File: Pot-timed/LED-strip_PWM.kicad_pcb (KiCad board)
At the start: 2 copper layers, 29.7 x 10 mm, 14 parts, among them IC1 ATTINY13A-MM, P1 CONN_2, P2 CONN_2, T1 AO3400, U1 MCP1804-SOT23-5

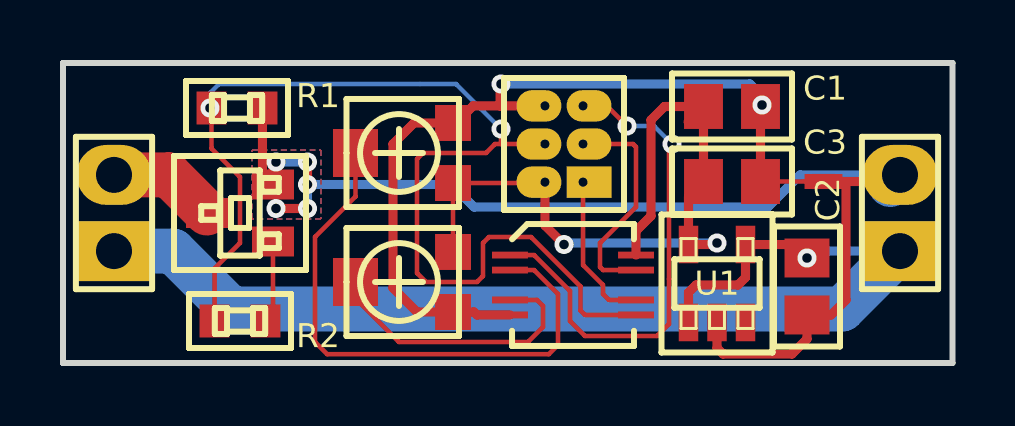
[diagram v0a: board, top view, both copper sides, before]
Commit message: Pot-timed: Attiny13 MLF10 (Unobtanium) --> MLF20.
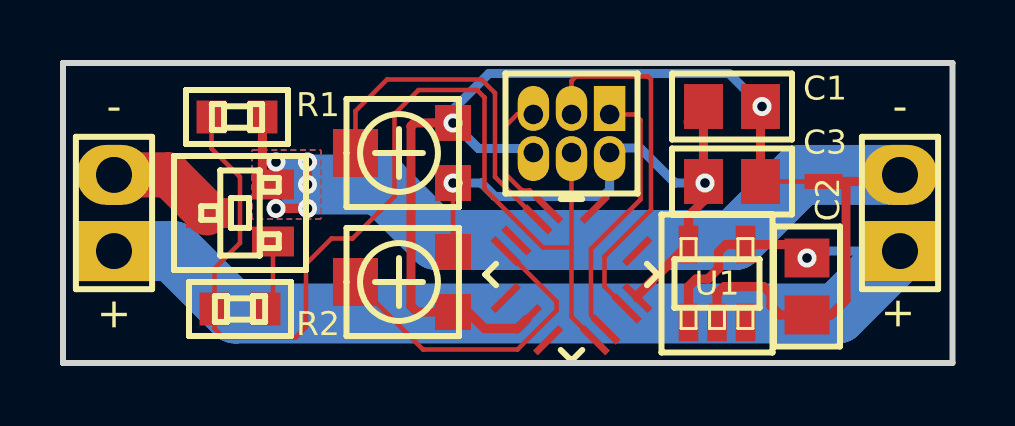
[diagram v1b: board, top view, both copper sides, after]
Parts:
- IC1: value ATTINY13A-MM -> ATTINY13-M; footprint MADW__MLF10 -> MADW__MLF20
- moved JP1 0.43 mm to (93.0, 50.4), turned to 180 degrees
- moved R2 0.40 mm to (81.9, 56.2)
- moved IC1 0.35 mm to (93.0, 55.0), turned to 315 degrees
- moved R1 0.30 mm to (81.8, 49.8)
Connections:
- IC1 pad 10: VCC -> (no net)
- IC1 pad 4: /POT2 -> (no net)
- IC1 pad 5: GND -> /POT2
- IC1 pad 6: /MOSI -> (no net)
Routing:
- net /RESET: track 16.7 -> 4.59 mm, vias 2 -> 0
- net /POT1: track 18.9 -> 11.5 mm
- net VCC: track 26.2 -> 21.2 mm
- net /SCK: track 7.55 -> 12.5 mm
- net /MISO: track 5.19 -> 8.98 mm
- net GND: track 29.0 -> 31.0 mm
- net /POT2: track 9.49 -> 10.9 mm
- net /MOSI: track 37.8 -> 37.3 mm, vias 2 -> 0
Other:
- board text added: "+"
- board text added: "-"

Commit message: Pot-timed: Found Attiny13 MLF10 at digikey...
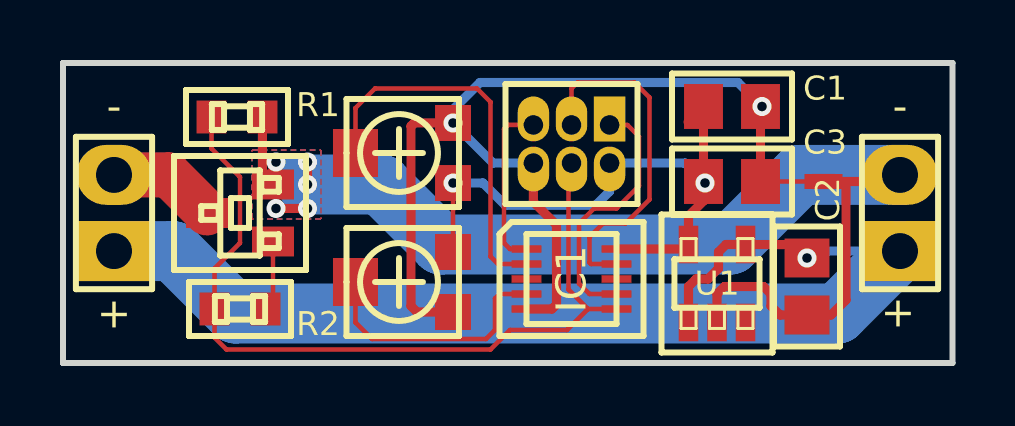
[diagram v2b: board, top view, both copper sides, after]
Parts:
- IC1: value ATTINY13-M -> ATTINY13A-MM; footprint MADW__MLF20 -> MADW__MLF10
- moved JP1 0.35 mm to (93.0, 50.7)
- moved IC1 0.15 mm to (93.0, 55.2), turned to 0 degrees
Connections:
- IC1 pad 10: (no net) -> VCC
- IC1 pad 4: (no net) -> /POT2
- IC1 pad 5: /POT2 -> GND
- IC1 pad 6: (no net) -> /MOSI
- IC1 pad 8: GND -> (no net)
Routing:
- net /MOSI: track 37.3 -> 28.1 mm
- net GND: track 31.0 -> 34.2 mm
- net /POT2: track 10.9 -> 8.51 mm
- net /POT1: track 11.5 -> 12.9 mm
- net /RESET: track 4.59 -> 5.67 mm
- net /SCK: track 12.5 -> 11.8 mm
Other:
- net class Power: clearance 0.2032 -> 0.1524
- board text added: "V0.10 POT PWM controller"
- board text removed: "V0.10 PWM controller"

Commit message: Pot-timed: Added an improvised center-pad to the MLF10 footprint.
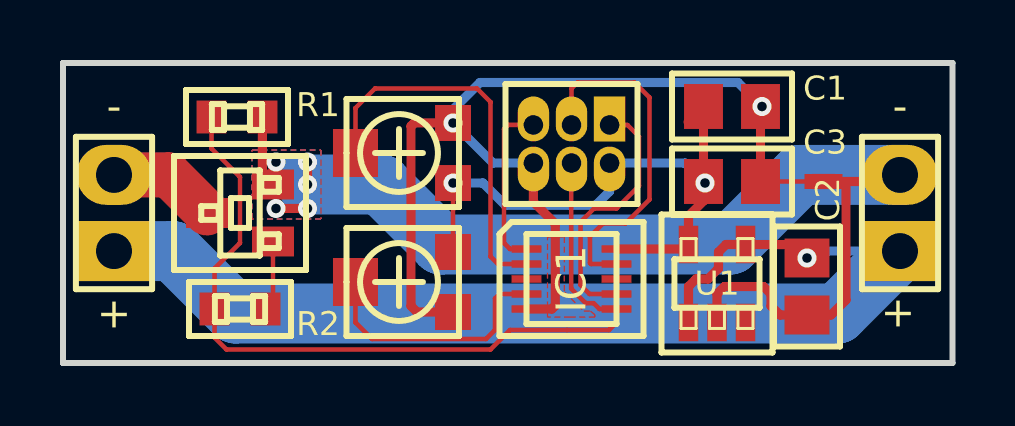
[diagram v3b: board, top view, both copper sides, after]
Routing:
- net /MOSI: track 28.1 -> 29.2 mm
- added copper zone on F.Cu, net GND
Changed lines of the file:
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@@
-(kicad_pcb (version 3) (host pcbnew "(2013-05-24 BZR 4164)-testing")
+(kicad_pcb (version 3) (host pcbnew "(2013-05-25 BZR 4168)-testing")
   (general
     (links 31)
@@
     (thickness 1.6002)
     (drawings 12)
-    (tracks 152)
+    (tracks 157)
     (zones 0)
     (modules 14)
@@
   )
   (layers
-    (15 Front signal hide)
+    (15 Front signal)
     (0 Back signal)
     (20 B.SilkS user)
-    (21 F.SilkS user hide)
+    (21 F.SilkS user)
     (22 B.Mask user)
     (23 F.Mask user)
@@
     (user_trace_width 2.5)
     (trace_clearance 0.1524)
-    (zone_clearance 0.25)
+    (zone_clearance 0.1524)
     (zone_45_only yes)
     (trace_min 0.1524)
@@
     (mod_text_size 0.8 0.8)
     (mod_text_width 0.2)
-    (pad_size 1.19888 1.19888)
-    (pad_drill 0)
+    (pad_size 1.64 2.6)
+    (pad_drill 0.5)
     (pad_to_mask_clearance 0)
     (aux_axis_origin 0 0)
@@
   (segment (start 95.2 52.1) (end 94.45 52.85) (width 0.1524) (layer Front) (net 1))
   (segment (start 94.45 52.85) (end 93.7 52.85) (width 0.1524) (layer Front) (net 1))
-  (segment (start 93.7 52.85) (end 93.2 53.35) (width 0.1524) (layer Front) (net 1))
-  (segment (start 93.2 53.35) (end 93.2 55.35) (width 0.1524) (layer Front) (net 1))
-  (segment (start 93.2 55.35) (end 93.55 55.7) (width 0.1524) (layer Front) (net 1))
+  (segment (start 93.7 52.85) (end 93.2508 53.2992) (width 0.1524) (layer Front) (net 1))
+  (segment (start 93.2508 53.2992) (end 93.2508 55.4008) (width 0.1524) (layer Front) (net 1))
+  (segment (start 93.2508 55.4008) (end 93.55 55.7) (width 0.1524) (layer Front) (net 1))
   (segment (start 94.45 55.7) (end 93.55 55.7) (width 0.1524) (layer Front) (net 1) (status 10))
   (segment (start 94.815 50.065) (end 94.22 50.065) (width 0.1524) (layer Front) (net 1) (status 20))
   (segment (start 95.2 50.45) (end 94.815 50.065) (width 0.1524) (layer Front) (net 1))
-  (segment (start 92.85 55.55) (end 92.85 51.435) (width 0.1524) (layer Front) (net 2) (status 20))
-  (segment (start 93.5 56.2) (end 92.85 55.55) (width 0.1524) (layer Front) (net 2))
-  (segment (start 92.85 51.435) (end 92.95 51.335) (width 0.1524) (layer Front) (net 2) (status 30))
-  (segment (start 93.5 56.2) (end 92.8 56.9) (width 0.1524) (layer Front) (net 2))
-  (segment (start 81.05164 57.15164) (end 81.05164 56.2) (width 0.1524) (layer Front) (net 2) (status 20))
+  (segment (start 92.8 56.9) (end 94.2 56.9) (width 0.1524) (layer Front) (net 2))
+  (segment (start 92.8 56.9) (end 90.9 56.9) (width 0.1524) (layer Front) (net 2))
+  (segment (start 90.9 56.9) (end 90.25 57.55) (width 0.1524) (layer Front) (net 2))
+  (segment (start 90.25 57.55) (end 81.45 57.55) (width 0.1524) (layer Front) (net 2))
   (segment (start 81.45 57.55) (end 81.05164 57.15164) (width 0.1524) (layer Front) (net 2))
-  (segment (start 90.25 57.55) (end 81.45 57.55) (width 0.1524) (layer Front) (net 2))
-  (segment (start 90.9 56.9) (end 90.25 57.55) (width 0.1524) (layer Front) (net 2))
-  (segment (start 92.8 56.9) (end 90.9 56.9) (width 0.1524) (layer Front) (net 2))
-  (segment (start 93.5 56.2) (end 94.45 56.2) (width 0.1524) (layer Front) (net 2) (status 20))
+  (segment (start 81.05164 56.2) (end 81.05164 57.15164) (width 0.1524) (layer Front) (net 2) (status 20))
+  (segment (start 94.45 56.65) (end 94.45 56.2) (width 0.1524) (layer Front) (net 2))
+  (segment (start 94.2 56.9) (end 94.45 56.65) (width 0.1524) (layer Front) (net 2))
+  (segment (start 92.95 51.335) (end 92.94 51.345) (width 0.1524) (layer Front) (net 2))
+  (segment (start 93.88 56.2) (end 94.45 56.2) (width 0.1524) (layer Front) (net 2))
+  (segment (start 93.684802 56.004802) (end 93.88 56.2) (width 0.1524) (layer Front) (net 2))
+  (segment (start 93.423746 56.004802) (end 93.684802 56.004802) (width 0.1524) (layer Front) (net 2))
+  (segment (start 92.94 55.521056) (end 93.423746 56.004802) (width 0.1524) (layer Front) (net 2))
+  (segment (start 92.94 51.345) (end 92.94 55.521056) (width 0.1524) (layer Front) (net 2))
+  (segment (start 92.9362 51.3488) (end 92.95 51.335) (width 0.1524) (layer Front) (net 2) (status 30))
   (segment (start 81.05164 56.6) (end 81.05164 54.84836) (width 0.1524) (layer Front) (net 2) (status 10))
   (segment (start 80.95164 50.85164) (end 80.95164 49.5) (width 0.1524) (layer Front) (net 2) (status 20))
@@
   (segment (start 90.7 50.2) (end 90.835 50.065) (width 0.1524) (layer Front) (net 5))
   (segment (start 92.95 50.065) (end 92.95 48.85) (width 0.1524) (layer Front) (net 6) (status 10))
-  (segment (start 93.6 54.7) (end 93.55 54.65) (width 0.1524) (layer Front) (net 6))
-  (segment (start 93.55 54.65) (end 93.55 53.8) (width 0.1524) (layer Front) (net 6))
-  (segment (start 93.55 53.8) (end 94 53.35) (width 0.1524) (layer Front) (net 6))
+  (segment (start 93.6 54.7) (end 93.5654 54.6654) (width 0.1524) (layer Front) (net 6))
+  (segment (start 93.5654 54.6654) (end 93.5654 53.7846) (width 0.1524) (layer Front) (net 6))
+  (segment (start 93.5654 53.7846) (end 94 53.35) (width 0.1524) (layer Front) (net 6))
   (segment (start 94 53.35) (end 94.75 53.35) (width 0.1524) (layer Front) (net 6))
   (segment (start 94.75 53.35) (end 95.55 52.55) (width 0.1524) (layer Front) (net 6))
@@
   (segment (start 91.68 51.335) (end 91.68 52.63) (width 0.3048) (layer Front) (net 9) (status 10))
   (segment (start 92.3 56.2) (end 91.45 56.2) (width 0.3048) (layer Front) (net 9) (status 20))
-  (segment (start 92.45 56.05) (end 92.3 56.2) (width 0.3048) (layer Front) (net 9))
-  (segment (start 92.45 53.4) (end 92.45 56.05) (width 0.3048) (layer Front) (net 9))
-  (segment (start 91.68 52.63) (end 92.45 53.4) (width 0.3048) (layer Front) (net 9))
+  (segment (start 92.41 56.09) (end 92.3 56.2) (width 0.3048) (layer Front) (net 9))
+  (segment (start 92.41 53.36) (end 92.41 56.09) (width 0.3048) (layer Front) (net 9))
+  (segment (start 91.68 52.63) (end 92.41 53.36) (width 0.3048) (layer Front) (net 9))
   (segment (start 99.3 49.45) (end 99.24996 49.45) (width 0.3048) (layer Front) (net 9) (status 30))
   (via (at 99.3 49.45) (size 0.635) (layers Front Back) (net 9) (status 30))
@@
       )
     )
+  )
+  (zone (net 0) (net_name "") (layer F.Mask) (hatch full 0.508)
+    (connect_pads (clearance 0.1524))
+    (min_thickness 0.1)
+    (fill (arc_segments 16) (thermal_gap 0.2032) (thermal_bridge_width 0.2032))
+    (polygon
+      (pts
+        (xy 92.15 53.8) (xy 92.71 53.8) (xy 92.71 55.63) (xy 93.36 56.27) (xy 93.58 56.27)
+        (xy 93.73 56.39) (xy 93.73 56.47) (xy 92.9 56.47) (xy 92.15 56.47)
+      )
+    )
+  )
+  (zone (net 9) (net_name GND) (layer Front) (hatch full 0.508)
+    (connect_pads (clearance 0.1524))
+    (min_thickness 0.1524)
+    (fill (arc_segments 16) (thermal_gap 0.2032) (thermal_bridge_width 0.2032))
+    (polygon
+      (pts
+        (xy 92.15 53.8) (xy 92.71 53.8) (xy 92.71 55.63) (xy 93.36 56.27) (xy 93.58 56.27)
+        (xy 93.73 56.39) (xy 93.73 56.47) (xy 92.9 56.47) (xy 92.15 56.47)
+      )
+    )

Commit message: Pot-timed: All 6-mil traces (except high-current ones).
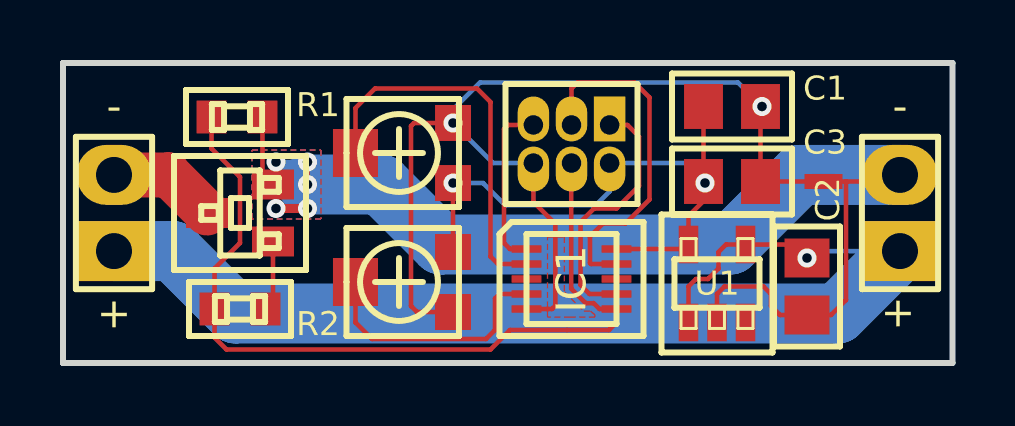
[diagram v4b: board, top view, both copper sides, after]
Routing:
- net VCC: track 20.7 -> 20.0 mm
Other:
- net class Power: trace_width 0.3048 -> 0.1524

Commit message: Pot-timed: Forgot logos. Panel now 100% V-groove.
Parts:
- added G1: OSHW-logo_silkscreen_3mm, OSHW-logo_silkscreen_3mm, B.Cu at (86.7, 52.2)
- added G2: LED_smile_silkscreen_3mm, LED_smile_silkscreen_3mm, B.Cu at (98.8, 52.2)

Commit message: Pot-timed: Layout tweaks (single board).
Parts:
- moved G2 2.25 mm to (96.5, 52.2)
- moved G1 1.25 mm to (85.5, 52.2)
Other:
- board text added: "12V"
- board text added: "LED"
- board text added: "V0.11 POT PWM controller"
- board text removed: "V0.10 POT PWM controller"
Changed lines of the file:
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@@
-(kicad_pcb (version 3) (host pcbnew "(2013-05-27 BZR 4172)-testing")
+(kicad_pcb (version 3) (host pcbnew "(2013-05-28 BZR 4174)-testing")
   (general
     (links 31)
@@
     (area 74.5076 46.6476 111.616669 61.100001)
     (thickness 1.6002)
-    (drawings 12)
+    (drawings 14)
     (tracks 156)
     (zones 0)
@@
     (title LED-strip_PWM)
     (date "24 May 2013")
-    (rev 0.1)
+    (rev 0.11)
     (company "2012 - blog.spitzenpfeil.org")
   )
@@
     (mod_text_size 0.8 0.8)
     (mod_text_width 0.2)
-    (pad_size 1.64 2.6)
-    (pad_drill 0.5)
+    (pad_size 4 2.5)
+    (pad_drill 1.2)
     (pad_to_mask_clearance 0)
     (pad_to_paste_clearance_ratio -0.06)
@@
     (fp_line (start 2.54 -1.27) (end 2.54 1.27) (layer F.SilkS) (width 0.2))
     (fp_line (start 2.54 1.27) (end -2.54 1.27) (layer F.SilkS) (width 0.2))
-    (pad 1 thru_hole rect (at -1.27 0 90) (size 2 2.5) (drill 1.2)
+    (pad 1 thru_hole rect (at -1.27 0 90) (size 4 2.5) (drill 1.2 (offset -1 0))
       (layers *.Cu *.Mask F.SilkS)
       (net 7 /Vin)
     )
-    (pad 2 thru_hole oval (at 1.27 0 90) (size 2 2.5) (drill 1.2)
+    (pad 2 thru_hole oval (at 1.27 0 90) (size 4 2.5) (drill 1.2 (offset 1 0))
       (layers *.Cu *.Mask F.SilkS)
       (net 10 GNDPWR)
@@
     (fp_line (start 2.54 -1.27) (end 2.54 1.27) (layer F.SilkS) (width 0.2))
     (fp_line (start 2.54 1.27) (end -2.54 1.27) (layer F.SilkS) (width 0.2))
-    (pad 1 thru_hole rect (at -1.27 0 90) (size 2 2.5) (drill 1.2)
+    (pad 1 thru_hole rect (at -1.27 0 90) (size 4 2.5) (drill 1.2 (offset -1 0))
       (layers *.Cu *.Mask F.SilkS)
       (net 7 /Vin)
     )
-    (pad 2 thru_hole oval (at 1.27 0 90) (size 2 2.5) (drill 1.2)
+    (pad 2 thru_hole oval (at 1.27 0 90) (size 4 2.5) (drill 1.2 (offset 1 0))
       (layers *.Cu *.Mask F.SilkS)
       (net 8 /drain)
@@
   )
   (module LED_smile_silkscreen_3mm (layer Back)
-    (at 98.75 52.2)
+    (at 96.5 52.2)
     (fp_text reference G2 (at 0 -1.7272) (layer B.SilkS) hide
       (effects (font (size 0.127 0.127) (thickness 0.00762)) (justify mirror))
@@
   )
   (module OSHW-logo_silkscreen_3mm (layer Back)
-    (at 86.7 52.2)
+    (at 85.45 52.2)
     (fp_text reference G1 (at 0 -1.59004) (layer B.SilkS) hide
       (effects (font (size 0.13462 0.13462) (thickness 0.0254)) (justify mirror))
@@
       (xy -0.90932 1.3462)) (layer B.SilkS) (width 0.00254))
   )
-  (gr_text + (at 77.7 56.35) (layer F.SilkS)
-    (effects (font (size 1 1) (thickness 0.2)))
-  )
-  (gr_text - (at 77.7 49.45) (layer F.SilkS)
-    (effects (font (size 1 1) (thickness 0.2)))
-  )
-  (gr_text - (at 103.9 49.45) (layer F.SilkS)
-    (effects (font (size 1 1) (thickness 0.2)))
-  )
-  (gr_text + (at 103.8 56.35 90) (layer F.SilkS)
-    (effects (font (size 1 1) (thickness 0.2)))
+  (gr_text + (at 79.7 55.25 90) (layer B.SilkS)
+    (effects (font (size 1 1) (thickness 0.2)) (justify mirror))
+  )
+  (gr_text - (at 79.7 50.775 90) (layer B.SilkS)
+    (effects (font (size 1 1) (thickness 0.2)) (justify mirror))
+  )
+  (gr_text LED (at 79.8 53 90) (layer B.SilkS)
+    (effects (font (size 0.8 0.8) (thickness 0.2)) (justify mirror))
+  )
+  (gr_text 12V (at 101.875 53 90) (layer B.SilkS)
+    (effects (font (size 0.8 0.8) (thickness 0.2)) (justify mirror))
+  )
+  (gr_text - (at 101.8 50.775 90) (layer B.SilkS)
+    (effects (font (size 1 1) (thickness 0.2)) (justify mirror))
+  )
+  (gr_text + (at 101.8 55.25 90) (layer B.SilkS)
+    (effects (font (size 1 1) (thickness 0.2)) (justify mirror))
   )
   (dimension 10 (width 0.2) (layer Cmts.User)
@@
   (gr_line (start 105.65 58) (end 105.65 48) (angle 90) (layer Edge.Cuts) (width 0.2))
   (gr_line (start 76 48) (end 76 58) (angle 90) (layer Edge.Cuts) (width 0.2))
-  (gr_text "V0.10\nPOT PWM controller" (at 92.8 53.2) (layer B.SilkS)
-    (effects (font (size 1.016 1.016) (thickness 0.2032)) (justify mirror))
-  )
-  (gr_text "2013 - blog.spitzenpfeil.org" (at 92.6 56.6) (layer B.SilkS)
-    (effects (font (size 1.016 1.016) (thickness 0.2032)) (justify mirror))
+  (gr_text "V0.11\nPOT PWM controller" (at 91 53.2) (layer B.SilkS)
+    (effects (font (size 1 1) (thickness 0.2032)) (justify mirror))
+  )
+  (gr_text "2013 - blog.spitzenpfeil.org" (at 91 56.6) (layer B.SilkS)
+    (effects (font (size 1 1) (thickness 0.2032)) (justify mirror))
   )
   (segment (start 95.2 52.1) (end 95.2 50.45) (width 0.1524) (layer Front) (net 1))
